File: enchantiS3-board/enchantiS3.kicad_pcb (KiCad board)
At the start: 4 copper layers, 55.9 x 25.4 mm, 60 parts, among them J1 USB_C_Receptacle_USB2.0, SW1 B3U-1000P, SW2 B3U-1000P, U1 USBLC6-2P6, U2 MCP73871, U3 NCP167AMX330TBG, U5 NCP167AMX330TBG, U6 MAX17262REWL+T, U7 LSM6DSV16XTR, U8 IIS2MDCTR

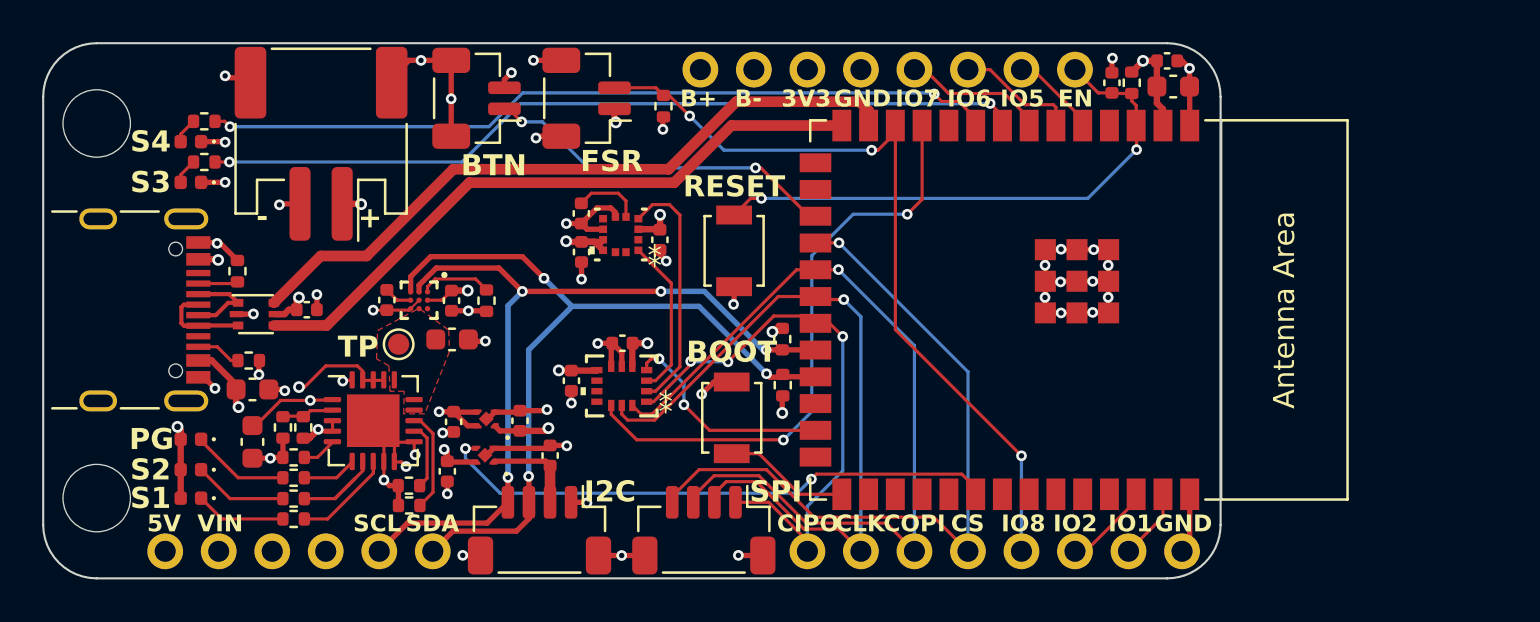
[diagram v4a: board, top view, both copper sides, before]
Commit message: added CAN transreceiver, cleaned up traces, added second jst header for FSR
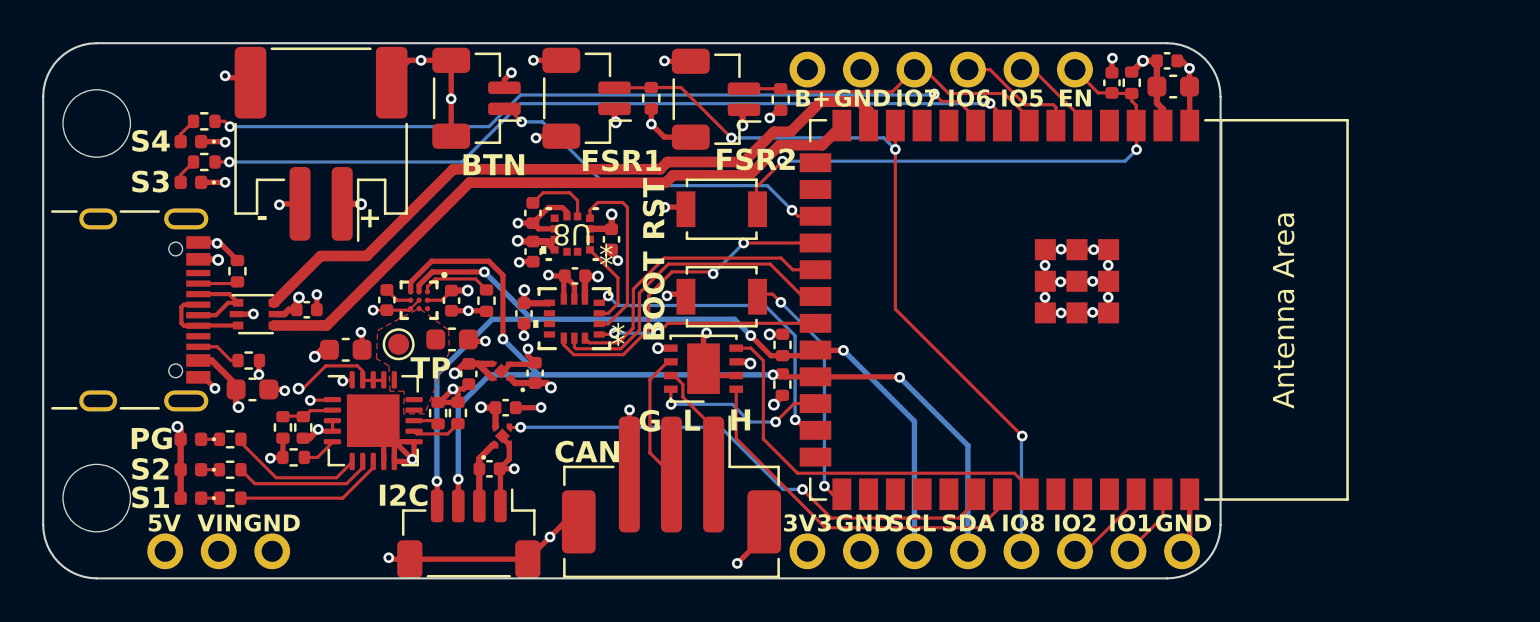
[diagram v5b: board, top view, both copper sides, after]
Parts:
- removed TOUCH2: JST-SH-1x04 1.0mm, Connector_JST:JST_SH_BM04B-SRSS-TB_1x04-1MP_P1.00mm_Vertical
- added ANG3: JST-SH-1.00mm 1x2, Connector_JST:JST_SH_BM02B-SRSS-TB_1x02-1MP_P1.00mm_Vertical, F.Cu at (124.6, 50.9)
- added G***: LOGO, logos:McGill_logo, B.Cu at (143.3, 66.6)
- added G***: LOGO, logos:IDMIL_logo, B.Cu at (146.3, 59.2)
- added J2: Conn_01x03_MountingPin, Connector_JST:JST_PH_B3B-PH-SM4-TB_1x03-1MP_P2.00mm_Vertical, F.Cu at (122.5, 69.2)
- added R2: 1k, Resistor_SMD:R_0402_1005Metric, F.Cu at (127.7, 50.9)
- added U9: TJA1051TK-3, Package_DFN_QFN:DFN-8-1EP_3x3mm_P0.65mm_EP1.55x2.4mm, F.Cu at (124.1, 63.7)
- moved C3 6.22 mm to (107.1, 62.8), turned to 0 degrees
- moved SW1 5.77 mm to (124.9, 60.3), turned to 180 degrees
- moved R20 4.59 mm to (111.5, 65.8), turned to -90 degrees
- moved R17 4.16 mm to (112.4, 65.8), turned to -90 degrees
- moved C17 4.10 mm to (114.7, 65.6), turned to 0 degrees
- moved C10 3.91 mm to (118.0, 59.3)
- moved U7 3.91 mm to (117.9, 61.3)
- moved C7 3.91 mm to (115.5, 61.1)
- moved R24 3.52 mm to (101.6, 67.1)
- moved TOUCH1 3.36 mm to (112.9, 71.5)
- moved R22 3.31 mm to (101.6, 68.5)
- moved R3 3.17 mm to (101.6, 69.9)
- moved C16 2.95 mm to (113.9, 68.5), turned to 0 degrees
- moved C5 2.38 mm to (116.1, 63.9)
- moved C4 2.38 mm to (112.9, 64.0)
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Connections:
- net /IO39 renamed /LDO_EN
- net /IO42 renamed /IO45
- BOARDLAYOUT1 pad 1.3: +3V3 -> /IO7
- BOARDLAYOUT1 pad 1.4: GND -> /IO6
- BOARDLAYOUT1 pad 1.5: /IO7 -> /IO5
- BOARDLAYOUT1 pad 1.6: /IO6 -> /EN
- BOARDLAYOUT1 pad 2.1: /CIPO -> +3V3
- BOARDLAYOUT1 pad 2.2: /SCLK -> GND
- BOARDLAYOUT1 pad 2.3: /COPI -> /SCL
- BOARDLAYOUT1 pad 2.4: /CS -> /SDA
- BOARDLAYOUT1 pad 3.3: +3V3 -> GND
- MCU1 pad 11: /CS1 -> /IO18
- MCU1 pad 24: unconnected-(MCU1-GPIO47/SPICLK_P/SUBSPICLK_P_DIFF-Pad24) -> /CAN_MODE
- MCU1 pad 31: unconnected-(MCU1-GPIO38/FSPIWP/SUBSPIWP-Pad31) -> /IO38
- MCU1 pad 33: /IO40 -> /CAN_TX
- MCU1 pad 34: /IO41 -> /CAN_RX
- U7 pad 12: /CS1 -> /CS
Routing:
- net /CS1: track 28.3 -> 0.00 mm, vias 2 -> 0
- net /COPI: track 40.3 -> 14.0 mm, vias 1 -> 0
- net GND: track 83.5 -> 106.1 mm, vias 50 -> 52
- net /SCLK: track 34.8 -> 15.2 mm, vias 1 -> 0
- net /CAN_RX: track 0.00 -> 19.1 mm
- net /CS: track 34.7 -> 15.7 mm, vias 1 -> 2
- net /CAN_TX: track 0.00 -> 17.7 mm
- net /CIPO: track 27.1 -> 10.5 mm, vias 3 -> 2
- net /IO7: track 6.75 -> 15.3 mm
- net /CAN_MODE: track 0.00 -> 8.28 mm, vias 0 -> 2
- net /SDA: track 38.8 -> 46.9 mm, vias 3 -> 4
- net /SCL: track 38.4 -> 45.2 mm
- net /CAN_L: track 0.00 -> 6.27 mm
- net /IO0: track 6.02 -> 11.8 mm, vias 0 -> 2
- net /CAN_H: track 0.00 -> 5.62 mm
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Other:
- board text added: "CAN"
- board text added: "EnchantiS3 v0.4 2024-05 Albert Niyonsenga"
- board text added: "FSR1"
- board text added: "FSR1 IO8"
- board text added: "FSR2"
- board text added: "FSR2 IO8"
- board text added: "G"
- board text added: "H"
- board text added: "L"
- board text added: "RST"
- board text removed: "B-"
- board text removed: "CIPO"
- board text removed: "CLK"
- board text removed: "COPI"
- board text removed: "CS"
- board text removed: "EVT1 = IO10 EVT2 = IO11 EVT3 = IO12 EVT4 = IO13"
- board text removed: "EnchantiS3 v0.3 2024-02 IDMIL McGill University Albert Niyonsenga"
- board text removed: "FSR"
- board text removed: "FSR IO8"
- board text removed: "RESET"
- board text removed: "SPI"

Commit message: changed color of board for 3D viewer
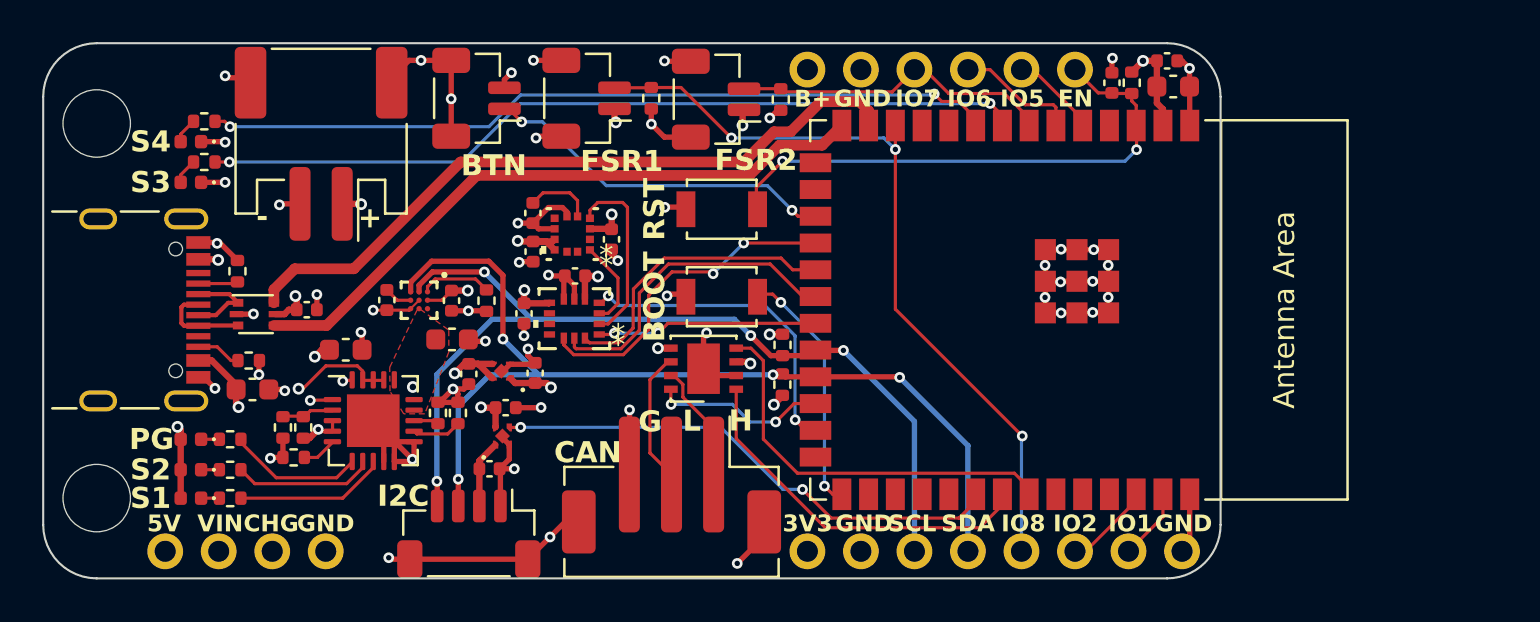
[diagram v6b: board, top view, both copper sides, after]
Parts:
- removed R20: 2k, Resistor_SMD:R_0402_1005Metric
- removed TH1: 10k, Resistor_SMD:R_0402_1005Metric
- removed TP1: TestPoint, TestPoint:TestPoint_Pad_D1.0mm
- added R11: 1k, Resistor_SMD:R_0402_1005Metric, F.Cu at (111.4, 65.8)
- added R14: 10k, Resistor_SMD:R_0402_1005Metric, F.Cu at (113.8, 60.5)
- moved G*** 11.5 mm to (134.3, 59.4)
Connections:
- BOARDLAYOUT1 pad 3.3: GND -> CHRG+
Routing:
- net CHRG+: track 0.01 -> 10.6 mm, vias 0 -> 1
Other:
- board text added: "CHG"
- board text added: "FSR2 IO7"
- board text removed: "FSR2 IO8"
- board text removed: "TP"

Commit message: switched battery charged and regulators
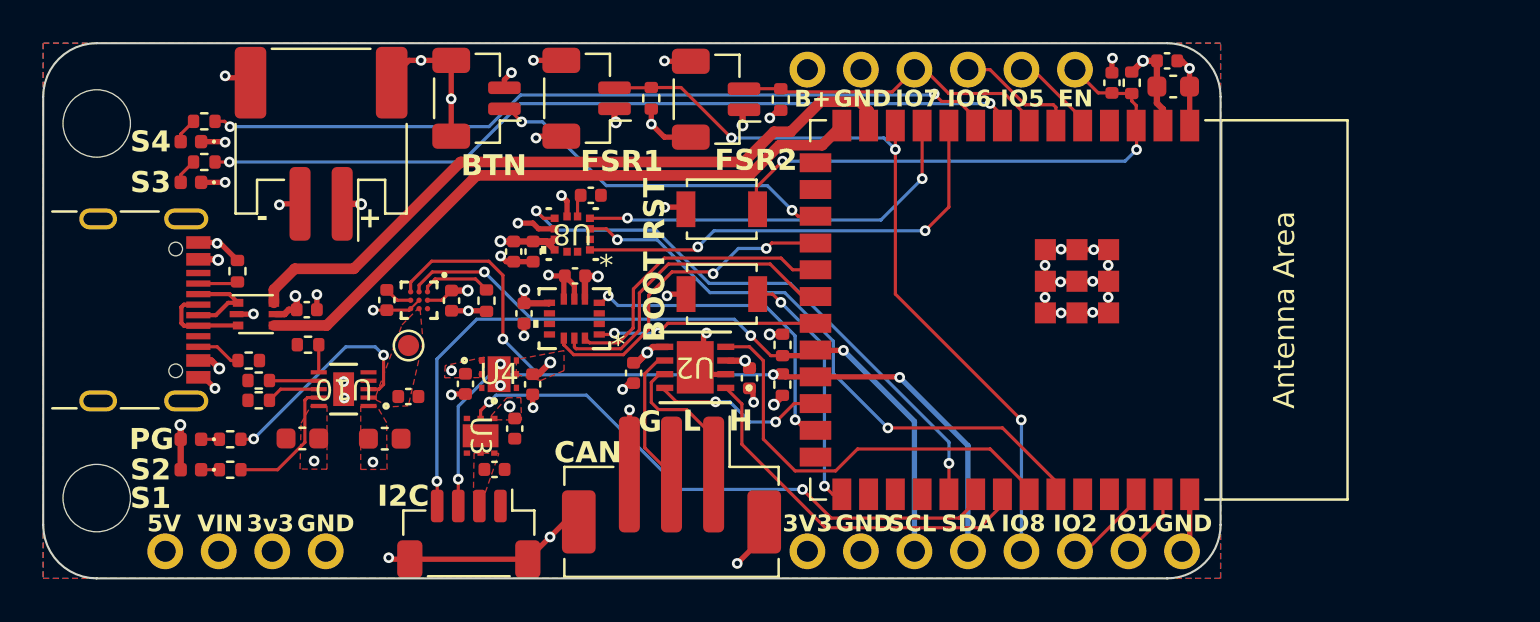
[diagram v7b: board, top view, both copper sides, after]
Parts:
- removed C14: 10uF, Capacitor_SMD:C_0603_1608Metric
- removed C16, C17: 1uF, Capacitor_SMD:C_0402_1005Metric
- removed CHARGLED3: PG, LED_SMD:LED_0402_1005Metric
- removed R11, R24: 1k, Resistor_SMD:R_0402_1005Metric
- removed R17: 24.9k, Resistor_SMD:R_0402_1005Metric
- removed R18: 330k, Resistor_SMD:R_0402_1005Metric
- removed R4: 110k, Resistor_SMD:R_0402_1005Metric
- removed R9: 10k, Resistor_SMD:R_0402_1005Metric
- removed U5: NCP167AMX330TBG, NCP167AMX330TBG-footprints:XDFN4_1X1_711AJ_ONS
- removed U9: TJA1051TK-3, Package_DFN_QFN:DFN-8-1EP_3x3mm_P0.65mm_EP1.55x2.4mm
- added C11: 1uF, Capacitor_SMD:C_0402_1005Metric, F.Cu at (112.8, 64.4)
- added C12: 1uF, Capacitor_SMD:C_0402_1005Metric, F.Cu at (115.9, 64.5)
- added C21: 10uF, Capacitor_SMD:C_0603_1608Metric, F.Cu at (105.0, 67.0)
- added C22: 1uF, Capacitor_SMD:C_0402_1005Metric, F.Cu at (110.0, 65.0)
- added C23: 10uF, Capacitor_SMD:C_0603_1608Metric, F.Cu at (108.9, 67.0)
- added R19: 0.43k, Resistor_SMD:R_0402_1005Metric, F.Cu at (102.9, 65.2)
- added R20: 13k, Resistor_SMD:R_0402_1005Metric, F.Cu at (102.9, 64.3)
- added R21: 10k, Resistor_SMD:R_0402_1005Metric, F.Cu at (105.3, 62.6)
- added TP1: TestPoint, TestPoint:TestPoint_Pad_D1.0mm, F.Cu at (110.0, 62.6)
- added U10: BQ25185DLHR, BQ25185-footprints:WSON10_DLH_TEX-M, F.Cu at (107.0, 64.7)
- added U4: NCV8187AMT330TAG, NCV8187-footprints:NCV8187AMT330TAG_ONS-L, F.Cu at (114.3, 64.0)
- C3: value 4.7uF -> 1uF; footprint Capacitor_SMD:C_0603_1608Metric -> Capacitor_SMD:C_0402_1005Metric
- C8: value 4.7uF -> 0.1uF; footprint Capacitor_SMD:C_0603_1608Metric -> Capacitor_SMD:C_0402_1005Metric
- U2: value MCP73871 -> PTCAN3413DRBR; footprint Package_DFN_QFN:QFN-20-1EP_4x4mm_P0.5mm_EP2.5x2.5mm -> TCAN3413-footprints:VSON8-DRB_TEX
- U3: value NCP167AMX330TBG -> NCV8187AMT330TAG; footprint NCP167AMX330TBG-footprints:XDFN4_1X1_711AJ_ONS -> NCV8187-footprints:NCV8187AMT330TAG_ONS-L
- moved U2 15.5 mm to (123.7, 63.6), turned to 180 degrees
- moved C8 14.2 mm to (126.2, 64.2), turned to -90 degrees
- moved C3 13.7 mm to (120.7, 63.9), turned to -90 degrees
- moved C5 4.97 mm to (114.1, 68.5), turned to 0 degrees
- moved C20 4.68 mm to (115.0, 58.2)
- moved C4 3.39 mm to (115.1, 66.5)
- moved U3 3.22 mm to (113.5, 66.9), turned to -90 degrees
- moved C18 2.87 mm to (118.7, 55.5), turned to 0 degrees
- moved CHARGLED2 1.44 mm to (99.7, 67.1)
- moved R22 1.44 mm to (101.6, 67.1)
- moved CHARGLED1 1.35 mm to (99.7, 68.5)
- moved R3 1.35 mm to (101.6, 68.5)
- moved SW1 0.12 mm to (124.9, 60.2)
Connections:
- net /IO15 renamed /BLUELED
- net /IO16 renamed /ORANGELED
- net /IO7 renamed /FSR2
- net /IO8 renamed /FSR1
- net /IO9 renamed /BTN
- BOARDLAYOUT1 pad 3.3: CHRG+ -> +3V3
- C3 pad 1: SYS -> +3V3
- C5 pad 1: +3V3 -> 3V3_AUX
- C8 pad 1: CHRG+ -> +3V3
- MCU1 pad 10: /IO17 -> /SPC
- MCU1 pad 11: /IO18 -> /SDIO
- MCU1 pad 31: /IO38 -> /MAG_INT
- MCU1 pad 35: /IO45 -> /CS1
- R3 pad 2: /STAT -> /STAT1
- U2 pad 1: SYS -> /CAN_TX
- U2 pad 2: /VPCC -> GND
- U2 pad 3: VUSB -> +3V3
- U2 pad 4: VUSB -> /CAN_RX
- U2 pad 5: /THERM -> +3V3
- U2 pad 6: /PG -> /CAN_L
- U2 pad 7: /STAT2 -> /CAN_H
- U2 pad 8: /STAT -> /CAN_MODE
- U3 pad 1: +3V3 -> SYS
- U3 pad 2: GND -> /LDO_EN
- U3 pad 3: SYS -> GND
- U3 pad 4: SYS -> unconnected-(U3-PG-Pad4)
- U3 pad 5: GND -> 3V3_AUX
- U7 pad 2: /SDA_EXT -> unconnected-(U7-SDx/AH1/QVAR1-Pad2)
- U7 pad 3: /SCL_EXT -> unconnected-(U7-SCx/AH2/QVAR2-Pad3)
- U8 pad 1: /SCL_EXT -> /SPC
- U8 pad 3: +3V3 -> /CS1
- U8 pad 4: /SDA_EXT -> /SDIO
- U8 pad 7: unconnected-(U8-INT/DRDY-Pad7) -> /MAG_INT
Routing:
- net /CS1: track 0.00 -> 28.6 mm, vias 0 -> 2
- net /MAG_INT: track 0.00 -> 27.7 mm, vias 0 -> 2
- net GND: track 106.1 -> 82.0 mm, vias 52 -> 50
- net /SPC: track 0.00 -> 21.7 mm, vias 0 -> 2
- net /SDIO: track 0.00 -> 19.1 mm, vias 0 -> 2
- net VUSB: track 21.3 -> 6.01 mm, vias 6 -> 5
- net CHRG+: track 10.6 -> 0.00 mm, vias 1 -> 0
- net /SDA_EXT: track 8.74 -> 0.00 mm
- net SYS: track 7.42 -> 0.01 mm, vias 5 -> 3
- net /STAT: track 7.17 -> 0.00 mm
- net /PG: track 6.44 -> 0.00 mm
- net /STAT1: track 0.00 -> 6.29 mm
- net /STAT2: track 6.66 -> 11.0 mm, vias 0 -> 2
- net /SCL_EXT: track 4.18 -> 0.00 mm
- net 3V3_AUX: track 3.22 -> 0.00 mm
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- added copper zone on F.Cu, net +3V3
- added copper zone on F.Cu, net 3V3_AUX
- added copper zone on B.Cu, net GND
- added copper zone on F.Cu, net GND
- added copper zone on F.Cu, net SYS
- added copper zone on F.Cu, net VUSB
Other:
- board text added: "3v3"
- board text removed: "CHG"

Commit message: Updated BOM and manufacturing files, removed CAN transceiver, updated silkscreen
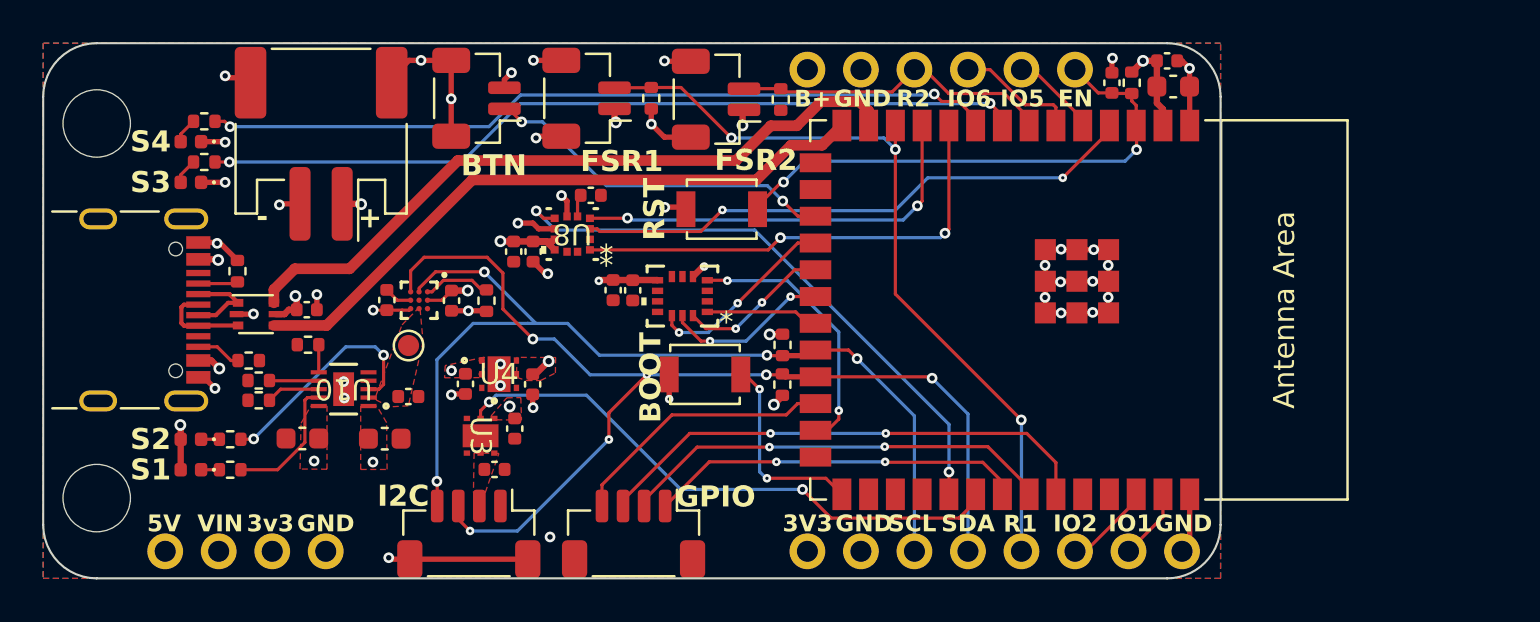
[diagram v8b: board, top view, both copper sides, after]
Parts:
- removed C3: 1uF, Capacitor_SMD:C_0402_1005Metric
- removed C8: 0.1uF, Capacitor_SMD:C_0402_1005Metric
- removed J2: Conn_01x03_MountingPin, Connector_JST:JST_PH_B3B-PH-SM4-TB_1x03-1MP_P2.00mm_Vertical
- removed U2: PTCAN3413DRBR, TCAN3413-footprints:VSON8-DRB_TEX
- added TOUCH2: JST-SH-1x04 1.0mm, Connector_JST:JST_SH_BM04B-SRSS-TB_1x04-1MP_P1.00mm_Vertical, F.Cu at (120.7, 71.5)
- moved U7 5.24 mm to (123.0, 60.3)
- moved C7 4.37 mm to (119.8, 60.0)
- moved SW1 3.89 mm to (124.1, 64.0)
- moved C10 2.82 mm to (120.7, 60.0), turned to -90 degrees
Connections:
- MCU1 pad 24: /CAN_MODE -> /EVT4
- MCU1 pad 33: /CAN_TX -> /EVT1
- MCU1 pad 34: /CAN_RX -> /EVT2
- MCU1 pad 35: /CS1 -> /EVT3
- MCU1 pad 4: /IO4 -> /CS1
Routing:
- net /EVT3: track 0.00 -> 24.2 mm, vias 0 -> 2
- net /EVT2: track 0.00 -> 20.7 mm, vias 0 -> 2
- net /CAN_RX: track 20.5 -> 0.00 mm
- net GND: track 82.0 -> 62.7 mm, vias 50 -> 42
- net /CAN_TX: track 18.0 -> 0.00 mm
- net /EVT1: track 0.00 -> 17.9 mm, vias 0 -> 2
- net /EVT4: track 0.00 -> 12.7 mm
- net /CAN_MODE: track 8.25 -> 0.00 mm, vias 2 -> 0
- net /SCLK: track 15.2 -> 7.89 mm, vias 0 -> 2
- net /CAN_H: track 7.18 -> 0.00 mm
- net /COPI: track 14.0 -> 7.23 mm, vias 0 -> 2
- net /CAN_L: track 6.66 -> 0.00 mm
- net /CS: track 15.7 -> 9.18 mm
- net /CIPO: track 10.5 -> 5.36 mm, vias 2 -> 0
- net /SDA: track 46.9 -> 52.0 mm, vias 4 -> 6
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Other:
- board text added: "EVT1 = GPIO40 EVT2 = GPIO41 EVT3 = GPIO42 EVT4 = GPIO47"
- board text added: "EnchantiS3 v0.4 2024-06 Albert Niyonsenga"
- board text added: "GPIO"
- board text added: "R1"
- board text added: "R2"
- board text removed: "CAN"
- board text removed: "EnchantiS3 v0.4 2024-05 Albert Niyonsenga"
- board text removed: "G"
- board text removed: "H"
- board text removed: "IO7"
- board text removed: "IO8"
- board text removed: "L"
- board text removed: "PG"
